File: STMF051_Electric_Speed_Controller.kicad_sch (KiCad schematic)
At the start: 4 parts

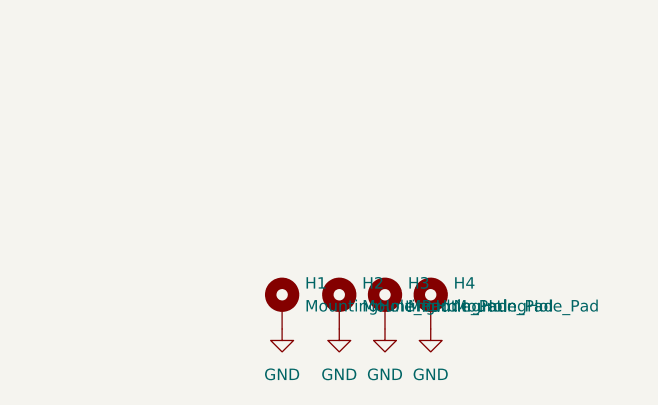
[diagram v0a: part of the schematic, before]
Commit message: cleanup layout, silkmasks, and add connections between planes for power and gnd
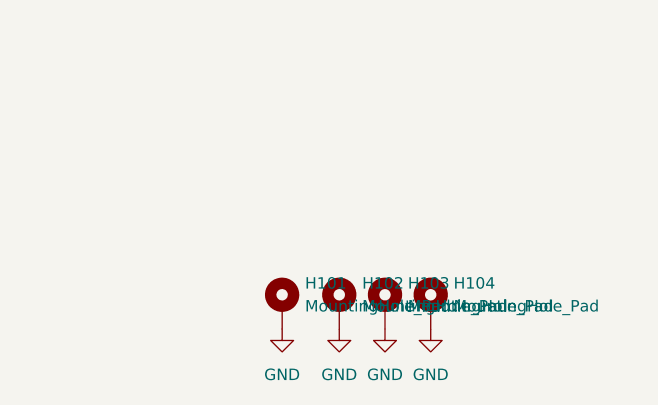
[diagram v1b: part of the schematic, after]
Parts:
- renumbered H1 to H101, H2 to H102, H3 to H103, H4 to H104
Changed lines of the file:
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@@
 		(dnp no)
 		(fields_autoplaced yes)
-		(property "Reference" "#PWR030"
+		(property "Reference" "#PWR0103"
 			(at 248.92 163.83 0)
 			(effects
@@
 			(project "ESC BB21"
 				(path "/d268946a-c85a-4346-a268-ba5c3792dae2"
-					(reference "#PWR030")
+					(reference "#PWR0103")
 					(unit 1)
 				)
@@
 		(dnp no)
 		(fields_autoplaced yes)
-		(property "Reference" "#PWR029"
+		(property "Reference" "#PWR0102"
 			(at 243.84 163.83 0)
 			(effects
@@
 			(project "ESC BB21"
 				(path "/d268946a-c85a-4346-a268-ba5c3792dae2"
-					(reference "#PWR029")
+					(reference "#PWR0102")
 					(unit 1)
 				)
@@
 		(dnp no)
 		(fields_autoplaced yes)
-		(property "Reference" "H3"
+		(property "Reference" "H103"
 			(at 251.46 152.3999 0)
 			(effects
@@
 			(project "ESC BB21"
 				(path "/d268946a-c85a-4346-a268-ba5c3792dae2"
-					(reference "H3")
+					(reference "H103")
 					(unit 1)
 				)
@@
 		(dnp no)
 		(fields_autoplaced yes)
-		(property "Reference" "H2"
+		(property "Reference" "H102"
 			(at 246.38 152.3999 0)
 			(effects
@@
 			(project "ESC BB21"
 				(path "/d268946a-c85a-4346-a268-ba5c3792dae2"
-					(reference "H2")
+					(reference "H102")
 					(unit 1)
 				)
@@
 		(dnp no)
 		(fields_autoplaced yes)
-		(property "Reference" "H4"
+		(property "Reference" "H104"
 			(at 256.54 152.3999 0)
 			(effects
@@
 			(project "ESC BB21"
 				(path "/d268946a-c85a-4346-a268-ba5c3792dae2"
-					(reference "H4")
+					(reference "H104")
 					(unit 1)
 				)
@@
 		(dnp no)
 		(fields_autoplaced yes)
-		(property "Reference" "#PWR031"
+		(property "Reference" "#PWR0104"
 			(at 254 163.83 0)
 			(effects
@@
 			(project "ESC BB21"
 				(path "/d268946a-c85a-4346-a268-ba5c3792dae2"
-					(reference "#PWR031")
+					(reference "#PWR0104")
 					(unit 1)
 				)
@@
 		(dnp no)
 		(fields_autoplaced yes)
-		(property "Reference" "#PWR028"
+		(property "Reference" "#PWR0101"
 			(at 237.49 163.83 0)
 			(effects
@@
 			(project "ESC BB21"
 				(path "/d268946a-c85a-4346-a268-ba5c3792dae2"
-					(reference "#PWR028")
+					(reference "#PWR0101")
 					(unit 1)
 				)
@@
 		(dnp no)
 		(fields_autoplaced yes)
-		(property "Reference" "H1"
+		(property "Reference" "H101"
 			(at 240.03 152.3999 0)
 			(effects
@@
 			(project ""
 				(path "/d268946a-c85a-4346-a268-ba5c3792dae2"
-					(reference "H1")
-					(unit 1)
-				)
+					(reference "H101")
+					(unit 1)
+				)
